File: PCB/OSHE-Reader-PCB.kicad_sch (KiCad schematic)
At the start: 0 parts

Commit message: added charging IC to schematic :)
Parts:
- added U1: MCP73837T-FCI/UN, MSOP10_MC_MCH, symbol ul_MCP73837T-FCI-UN:MCP73837T-FCI_UN
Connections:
- new net +BATT: U1.10 (VBAT)
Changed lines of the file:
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@@
 	(generator_version "9.0")
 	(paper "A4")
+	(wire
+		(pts
+			(xy 118.11 44.45) (xy 118.11 46.99)
+		)
+		(stroke
+			(width 0)
+			(type default)
+		)
+	)
+	(wire
+		(pts
+			(xy 118.11 46.99) (xy 115.57 46.99)
+		)
+		(stroke
+			(width 0)
+			(type default)
+		)
+	)
+	(symbol
+		(lib_id "power:+BATT")
+		(at 118.11 44.45 0)
+		(unit 1)
+		(exclude_from_sim no)
+		(in_bom yes)
+		(on_board yes)
+		(dnp no)
+		(fields_autoplaced yes)
+		(property "Reference" "#PWR01"
+			(at 118.11 48.26 0)
+			(effects
+				(font
+					(size 1.27 1.27)
+				)
+				(hide yes)
+			)
+		)
+		(property "Value" "+BATT"
+			(at 118.11 39.37 0)
+			(effects
+				(font
+					(size 1.27 1.27)
+				)
+			)
+		)
+		(property "Footprint" ""
+			(at 118.11 44.45 0)
+			(effects
+				(font
+					(size 1.27 1.27)
+				)
+				(hide yes)
+			)
+		)
+		(property "Datasheet" ""
+			(at 118.11 44.45 0)
+			(effects
+				(font
+					(size 1.27 1.27)
+				)
+				(hide yes)
+			)
+		)
+		(property "Description" "Power symbol creates a global label with name \"+BATT\""
+			(at 118.11 44.45 0)
+			(effects
+				(font
+					(size 1.27 1.27)
+				)
+				(hide yes)
+			)
+		)
+		(pin "1"
+		)
+		(instances
+			(project ""
+				(path "/3f072c92-e35a-4654-839b-728bd3dc3a46"
+					(reference "#PWR01")
+					(unit 1)
+				)
+			)
+		)
+	)
+	(symbol
+		(lib_id "ul_MCP73837T-FCI-UN:MCP73837T-FCI_UN")
+		(at 49.53 46.99 0)
+		(unit 1)
+		(exclude_from_sim no)
+		(in_bom yes)
+		(on_board yes)
+		(dnp no)
+		(fields_autoplaced yes)
+		(property "Reference" "U1"
+			(at 82.55 36.83 0)
+			(effects
+				(font
+					(size 1.524 1.524)
+				)
+			)
+		)
+		(property "Value" "MCP73837T-FCI/UN"
+			(at 82.55 39.37 0)
+			(effects
+				(font
+					(size 1.524 1.524)
+				)
+			)
+		)
+		(property "Footprint" "MSOP10_MC_MCH"
+			(at 49.53 46.99 0)
+			(effects
+				(font
+					(size 1.27 1.27)
+					(italic yes)
+				)
+				(hide yes)
+			)
+		)
+		(property "Datasheet" "MCP73837T-FCI/UN"
+			(at 49.53 46.99 0)
+			(effects
+				(font
+					(size 1.27 1.27)
+					(italic yes)
+				)
+				(hide yes)
+			)
+		)
+		(property "Description" ""
+			(at 49.53 46.99 0)
+			(effects
+				(font
+					(size 1.27 1.27)
+				)
+				(hide yes)
+			)
+		)
+		(pin "7"
+		)
+		(pin "6"
+		)
+		(pin "10"
+		)
+		(pin "9"
+		)
+		(pin "8"
+		)
+		(pin "5"
+		)
+		(pin "4"
+		)
+		(pin "3"
+		)
+		(pin "2"
+		)
+		(pin "1"
+		)
+		(instances
+			(project ""
+				(path "/3f072c92-e35a-4654-839b-728bd3dc3a46"
+					(reference "U1")
+					(unit 1)
+				)
+			)
+		)
+	)
 	(sheet_instances
 		(path "/"

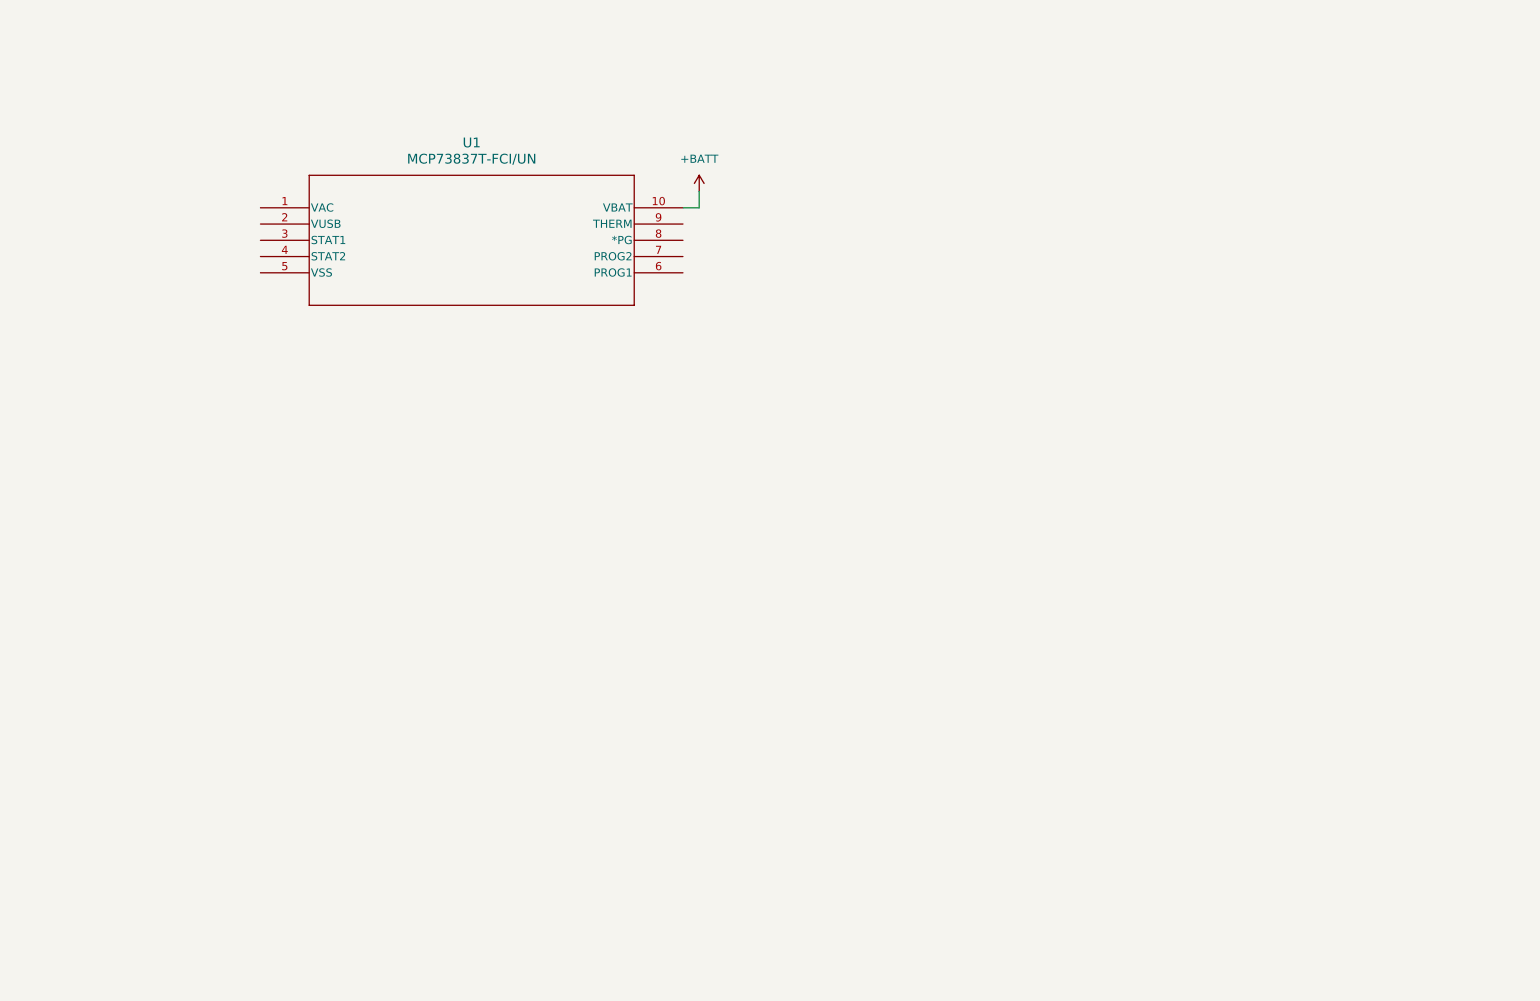
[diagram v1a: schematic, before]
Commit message: Added battery charging and power selector circuit to schematic, added symbols and footprints for BQ2057CSNTR, removed symbols and footprints for unused MCP73837T
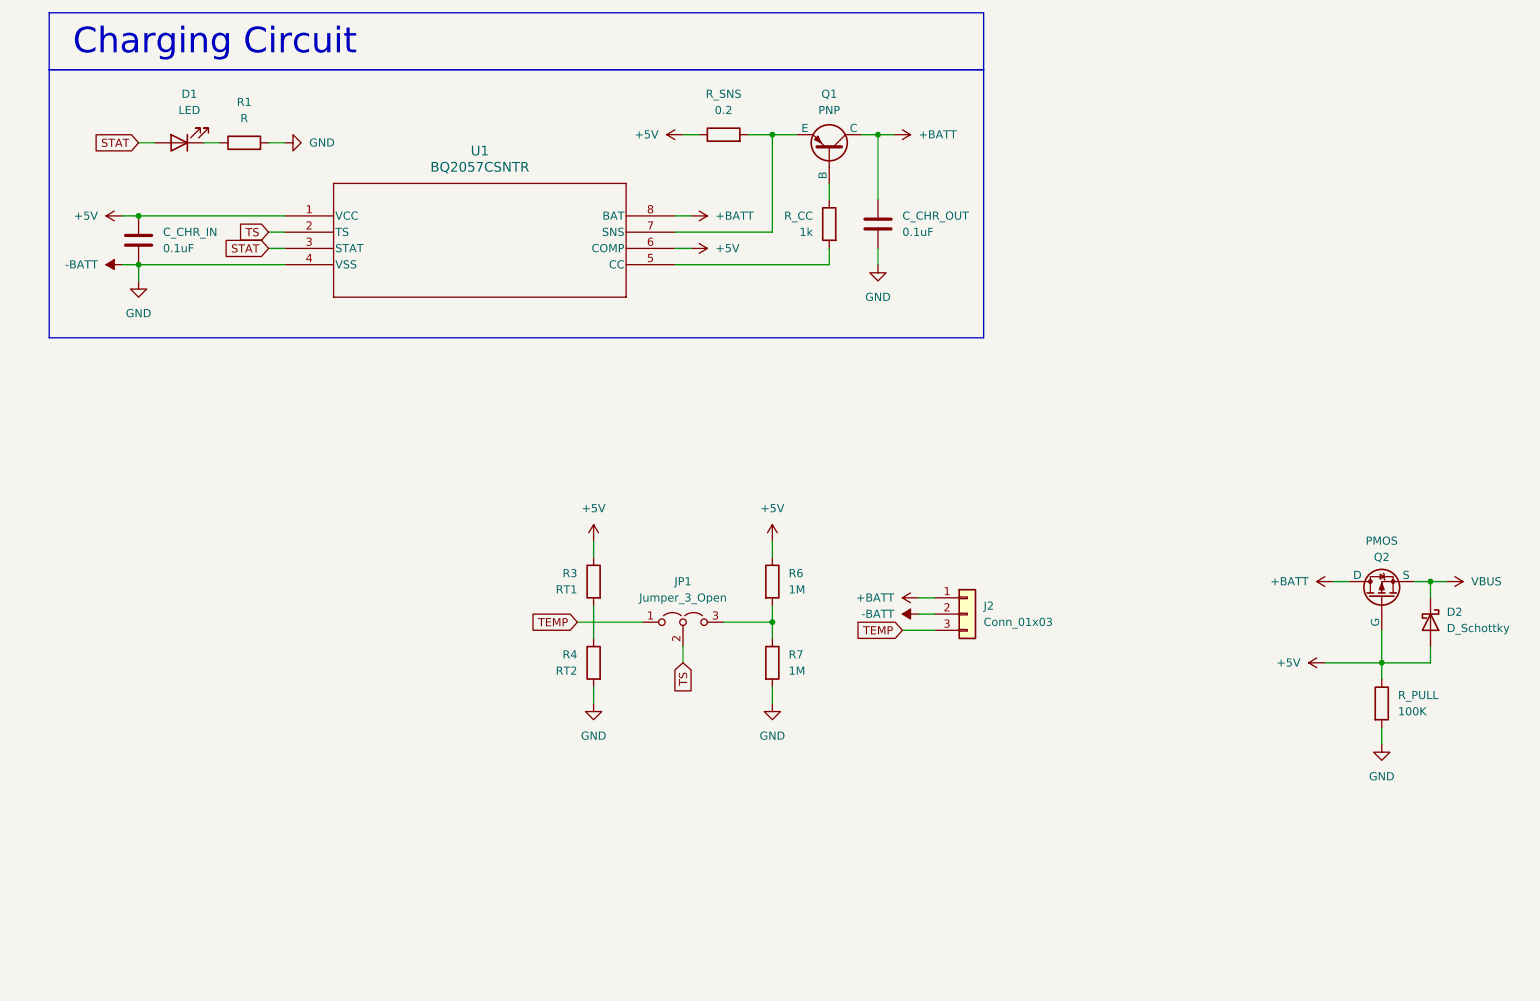
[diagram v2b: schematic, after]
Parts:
- removed U1: MCP73837T-FCI/UN, MSOP10_MC_MCH, symbol ul_MCP73837T-FCI-UN:MCP73837T-FCI_UN
- added C_CHR_IN, C_CHR_OUT: 0.1uF, symbol Device:C
- added D1: LED, symbol Device:LED
- added D2: D_Schottky, symbol Device:D_Schottky
- added J2: Conn_01x03, symbol Connector_Generic:Conn_01x03
- added JP1: Jumper_3_Open, symbol Jumper:Jumper_3_Open
- added Q1: PNP, symbol Simulation_SPICE:PNP
- added Q2: PMOS, symbol Simulation_SPICE:PMOS
- added R1: R, symbol Device:R
- added R3: RT1, symbol Device:R
- added R4: RT2, symbol Device:R
- added R6, R7: 1M, symbol Device:R
- added R_CC: 1k, symbol Device:R
- added R_PULL: 100K, symbol Device:R
- added R_SNS: 0.2, symbol Device:R
- added U1: BQ2057CSNTR, D8, symbol BQ2057CSNTR:BQ2057CSNTR
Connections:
- net +BATT: now also C_CHR_OUT.1, J2.1 (Pin_1), Q1.1 (C), Q2.1 (D), U1.8 (BAT)
- new net: R3.2, R4.1
- new net: D1.1 (K), R1.1
- new net: JP1.3 (B), R6.2, R7.1
- new net: Q1.2 (B), R_CC.1
- new net: Q1.3 (E), R_SNS.2, U1.7 (SNS)
- new net: R_CC.2, U1.5 (CC)
- new net +5V: C_CHR_IN.1, D2.2 (A), Q2.2 (G), R3.1, R6.1, R_PULL.1, R_SNS.1, U1.1 (VCC), U1.6 (COMP)
- new net -BATT: C_CHR_IN.2, C_CHR_OUT.2, J2.2 (Pin_2), R1.2, R4.2, R7.2, R_PULL.2, U1.4 (VSS)
- new net STAT: D1.2 (A), U1.3 (STAT)
- new net TEMP: J2.3 (Pin_3), JP1.1 (A)
- new net TS: JP1.2 (C), U1.2 (TS)
- new net VBUS: D2.1 (K), Q2.3 (S)
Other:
- note added: "Charging Circuit"

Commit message: relabeled groups, added indicator LED
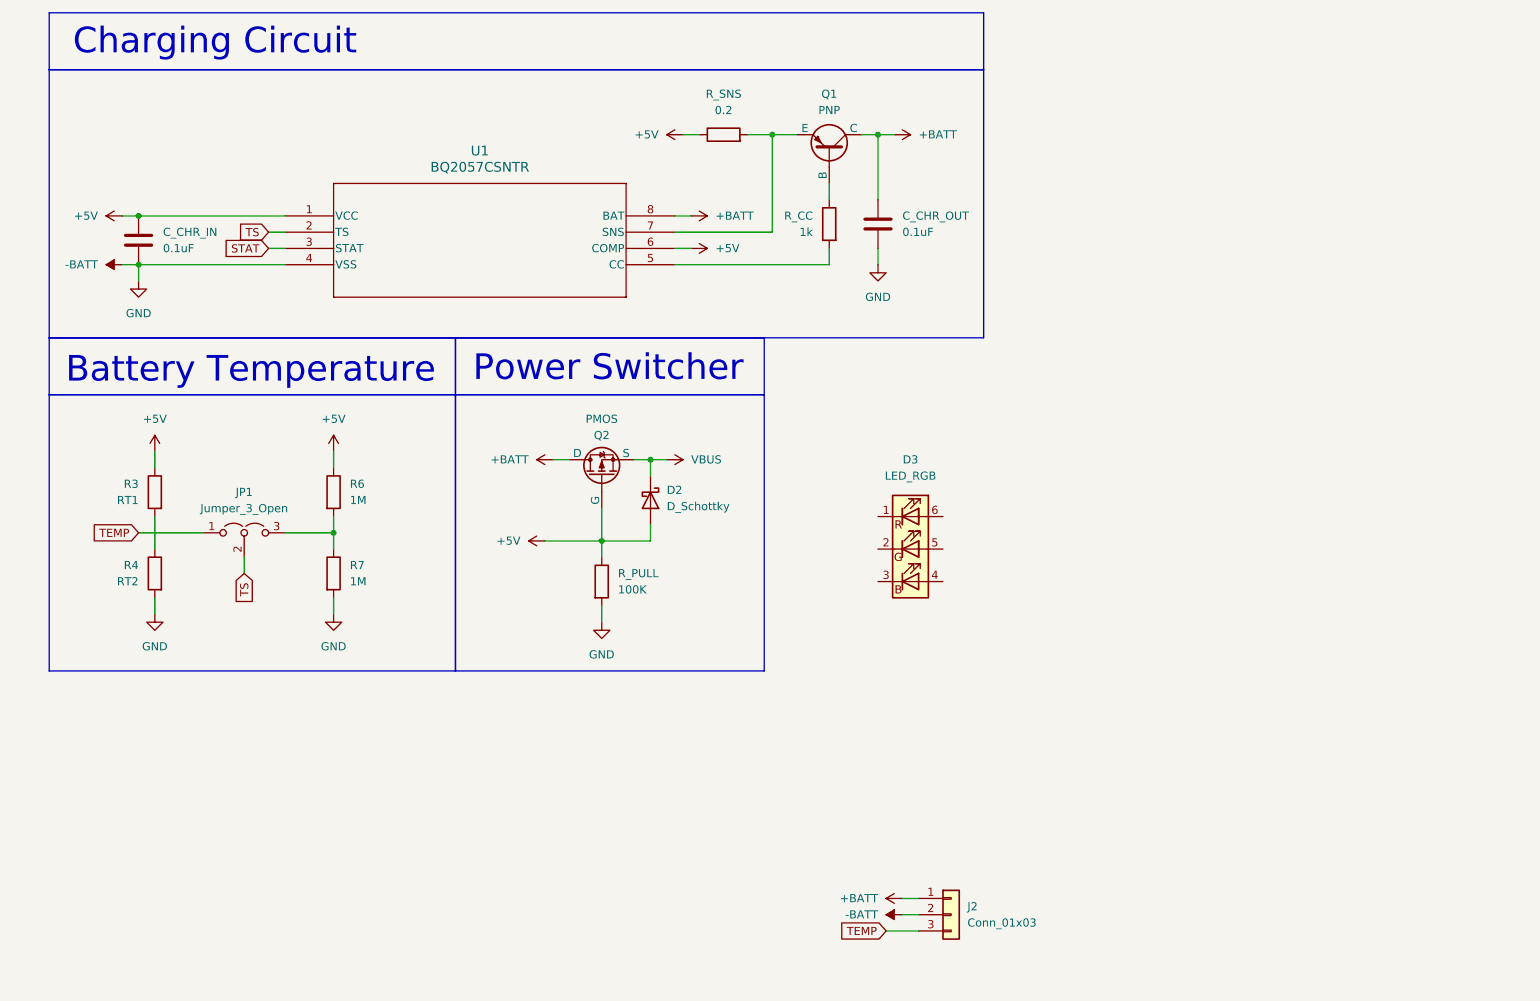
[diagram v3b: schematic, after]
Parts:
- removed D1: LED, symbol Device:LED
- removed R1: R, symbol Device:R
- added D3: LED_RGB, symbol Device:LED_RGB
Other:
- note added: "Battery Temperature"
- note added: "Power Switcher"
- moved on the sheet: D2, J2, JP1, Q2, R3, R4, R6, R7, R_PULL

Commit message: split pcb up into hierarchical files, playing with power flags and ERC
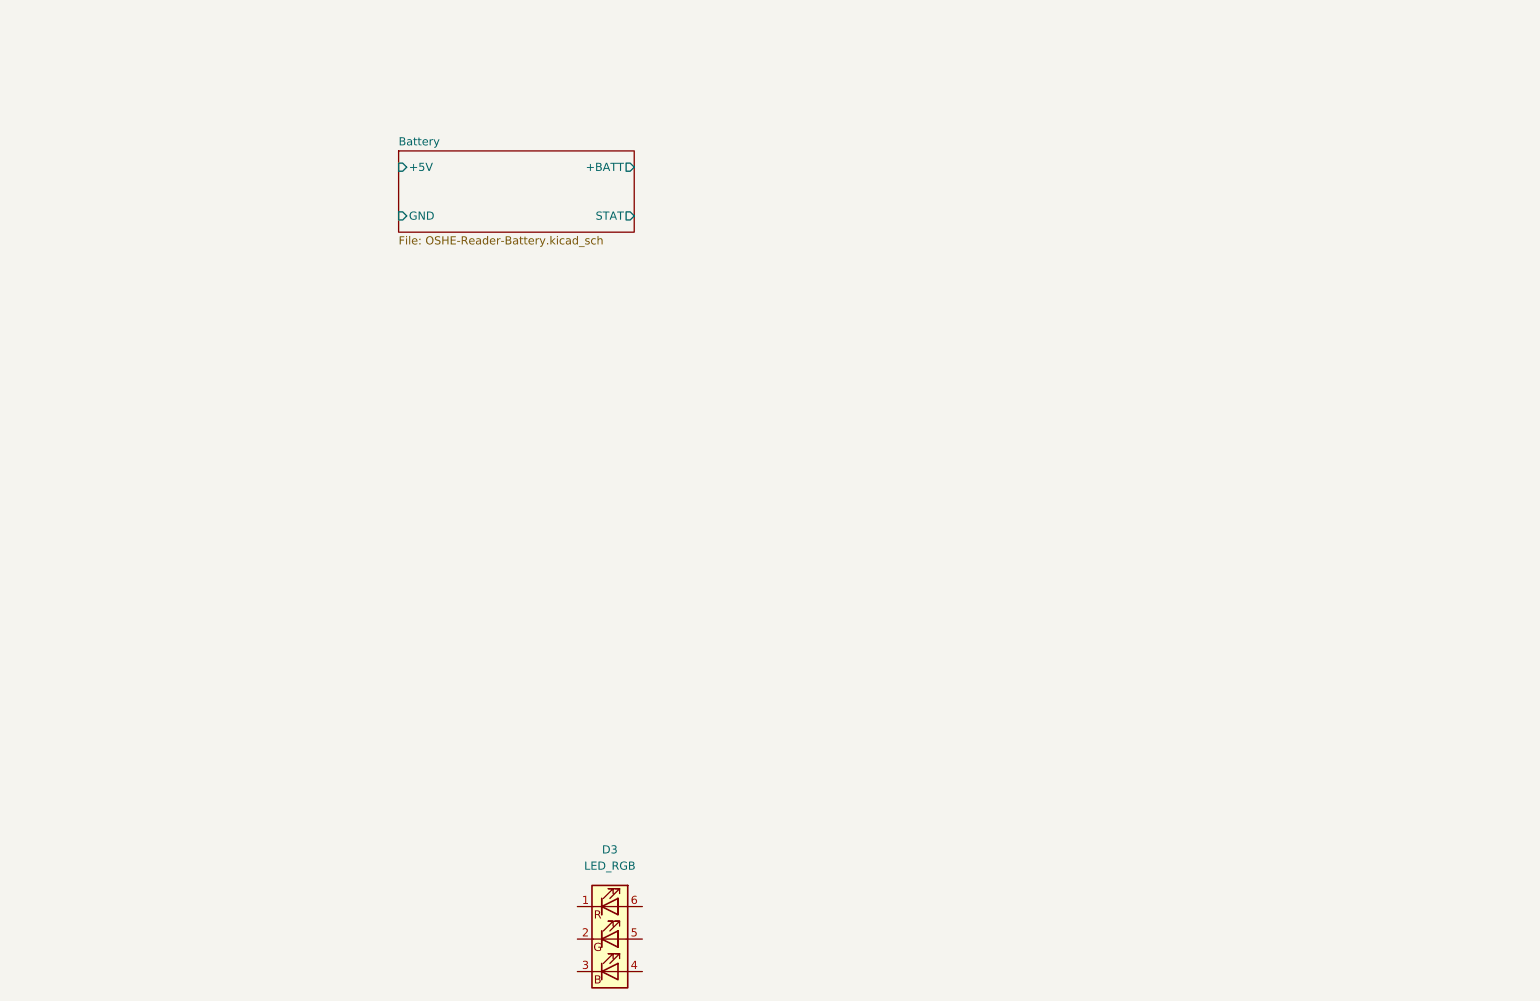
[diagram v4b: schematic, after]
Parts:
- removed C_CHR_IN, C_CHR_OUT: 0.1uF, symbol Device:C
- removed D2: D_Schottky, symbol Device:D_Schottky
- removed J2: Conn_01x03, symbol Connector_Generic:Conn_01x03
- removed JP1: Jumper_3_Open, symbol Jumper:Jumper_3_Open
- removed Q1: PNP, symbol Simulation_SPICE:PNP
- removed Q2: PMOS, symbol Simulation_SPICE:PMOS
- removed R3: RT1, symbol Device:R
- removed R4: RT2, symbol Device:R
- removed R6, R7: 1M, symbol Device:R
- removed R_CC: 1k, symbol Device:R
- removed R_PULL: 100K, symbol Device:R
- removed R_SNS: 0.2, symbol Device:R
- removed U1: BQ2057CSNTR, D8, symbol BQ2057CSNTR:BQ2057CSNTR
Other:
- added sheet Battery (OSHE-Reader-Battery.kicad_sch)
- note removed: "Battery Temperature"
- note removed: "Charging Circuit"
- note removed: "Power Switcher"
- moved on the sheet: D3

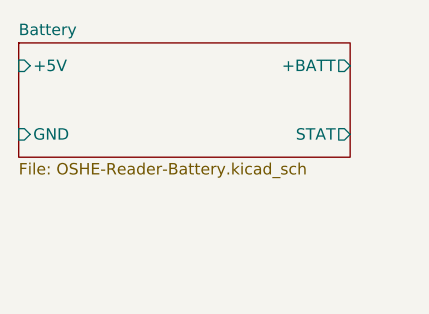
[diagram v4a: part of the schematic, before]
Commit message: changed sheet name from Battery to Battery-Charger
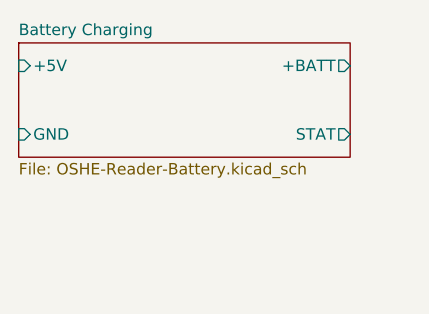
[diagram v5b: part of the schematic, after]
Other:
- sheet Battery renamed Battery Charging
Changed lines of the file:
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@@
 			(color 0 0 0 0.0000)
 		)
-		(property "Sheetname" "Battery"
+		(property "Sheetname" "Battery Charging"
 			(at 71.12 37.3884 0)
 			(effects

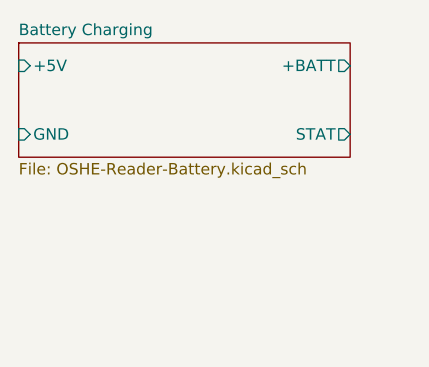
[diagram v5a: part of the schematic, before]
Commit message: added VBUS port on battery-charger section
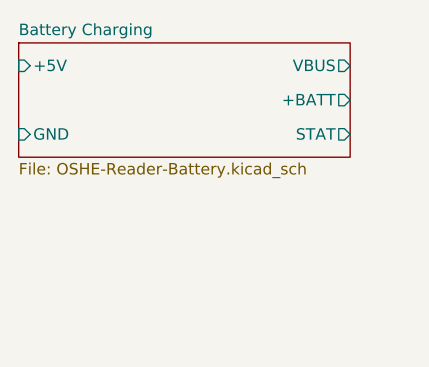
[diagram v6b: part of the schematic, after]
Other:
- sheet Battery Charging ports: added VBUS; removed none
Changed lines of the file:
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@@
 		)
 		(pin "+BATT" output
-			(at 107.95 40.64 0)
+			(at 107.95 44.45 0)
 			(effects
 				(font
@@
 			(effects
 				(font
+					(size 1.27 1.27)
+				)
+				(justify right)
+			)
+		)
+		(pin "VBUS" output
+			(at 107.95 40.64 0)
+			(effects
+				(font

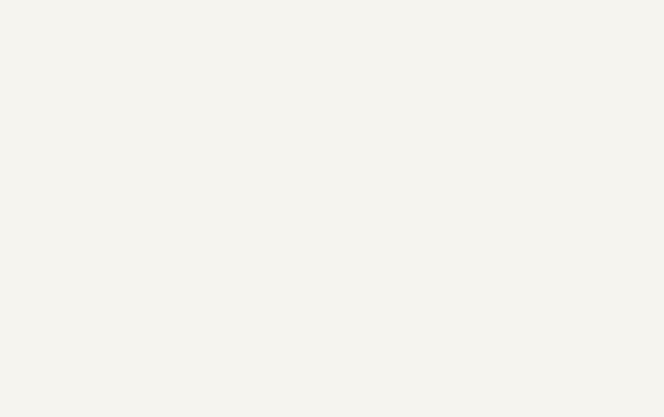
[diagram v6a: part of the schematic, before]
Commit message: Added Buck Converter to Schematic.
added buck converter, and hooked it up. In theroy should work from, 3.7-3.5 volts inputed, and output 3.3 volts
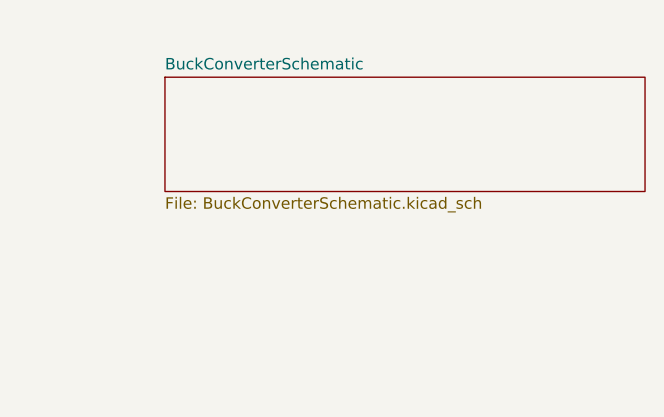
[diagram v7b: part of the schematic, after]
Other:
- added sheet BuckConverterSchematic (BuckConverterSchematic.kicad_sch)
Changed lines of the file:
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@@
+	)
+	(sheet
+		(at 172.72 41.91)
+		(size 53.34 12.7)
+		(exclude_from_sim no)
+		(in_bom yes)
+		(on_board yes)
+		(dnp no)
+		(fields_autoplaced yes)
+		(stroke
+			(width 0.1524)
+			(type solid)
+		)
+		(fill
+			(color 0 0 0 0.0000)
+		)
+		(property "Sheetname" "BuckConverterSchematic"
+			(at 172.72 41.1984 0)
+			(effects
+				(font
+					(size 1.27 1.27)
+				)
+				(justify left bottom)
+			)
+		)
+		(property "Sheetfile" "BuckConverterSchematic.kicad_sch"
+			(at 172.72 55.1946 0)
+			(effects
+				(font
+					(size 1.27 1.27)
+				)
+				(justify left top)
+			)
+		)
+		(instances
+			(project "OSHE-Reader-PCB"
+				(path "/3f072c92-e35a-4654-839b-728bd3dc3a46"
+					(page "3")
+				)
+			)
+		)
 	)
 	(sheet
